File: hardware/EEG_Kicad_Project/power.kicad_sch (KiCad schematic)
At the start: 32 parts, among them U2 TPS60403DBV, U4 TPS73225DBVT, U5 TLV75709PDBV, U6 TPS72325DBVT

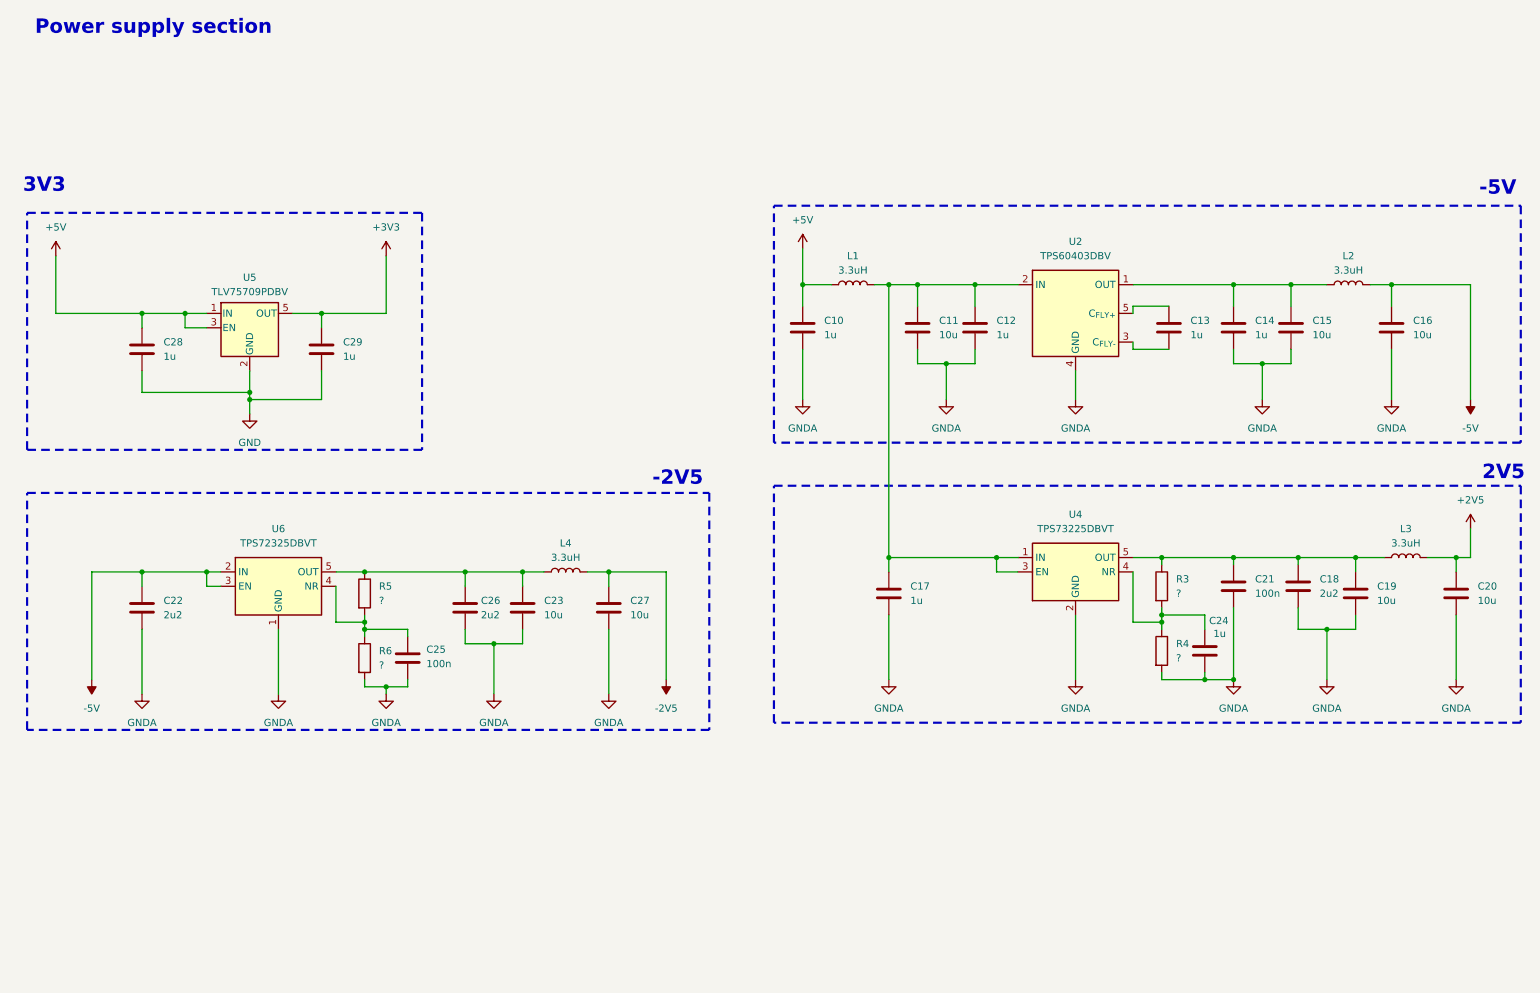
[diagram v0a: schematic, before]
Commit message: Add USB galvanic isolation barrier for patient safety
Adds a USB-C receptacle -> ESD protection -> ADuM3160 isolator ->
isolated TMU3-0511 DC-DC chain, separating the STM32/ADS1299/analog
supply (now fully isolated) from the non-isolated USB-connector side.
Closes the previously-floating USB_OTG_FS_DP/DM pins on the STM32,
adds CC1/CC2 pulldowns and VBUS decoupling on the new receptacle, and
fixes ADuM3160 VBUS2 tie per datasheet. Verified via kicad-happy: no
ERC regressions, isolation barrier confirmed intact (no net bridges
GND_PRI/+5V_PRI with the isolated GNDA/+5V/+3V3 domain).

Co-Authored-By: Claude Sonnet 5 <noreply@anthropic.com>
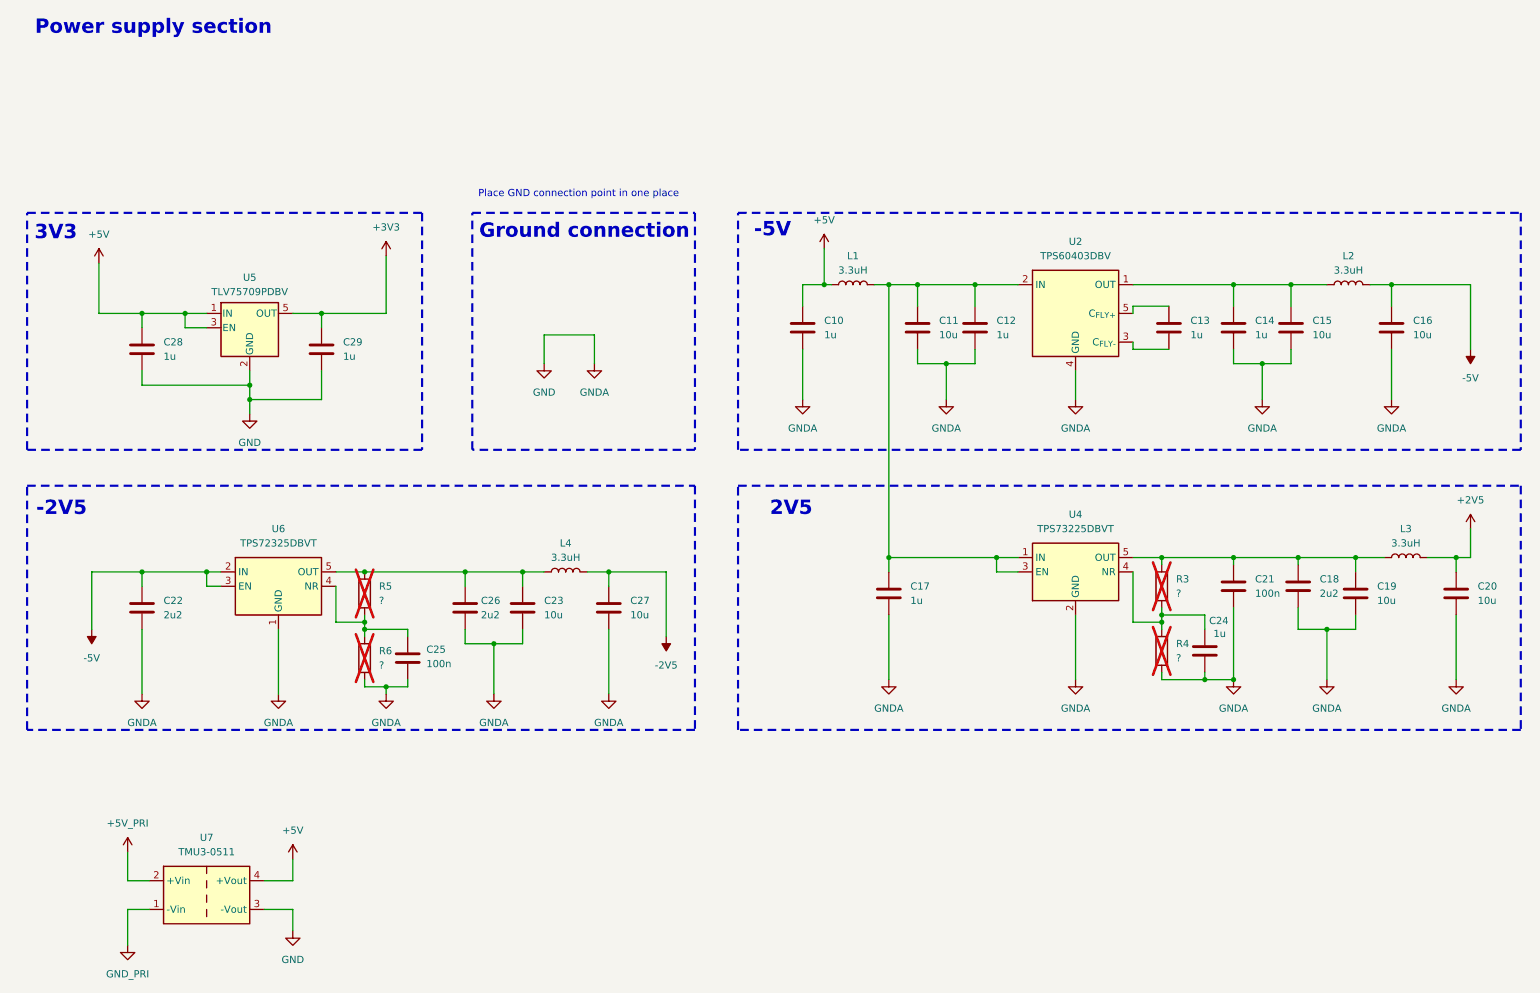
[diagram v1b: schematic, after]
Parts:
- added U7: TMU3-0511, Converter_DCDC:Converter_DCDC_TRACO_TMU3-05xx_12xx_THT, symbol Converter_DCDC:TMU3-0511
- R3, R4, R5, R6: now not fitted; now left out of the parts list
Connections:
- net GNDA is gone; now on net GND: C10.2, C11.2, C12.2, C14.2, C15.2, C16.2, C17.2, C18.2, C19.2, C20.2, C21.2, C22.2, C23.2, C24.2, C25.2, C26.2, C27.2, R4.2, R6.2, U2.4 (GND), U4.2 (GND), U6.1 (GND)
- net +5V: now also U7.4 (+Vout)
- net GND: now also U7.3 (-Vout)
- new net +5V_PRI: U7.2 (+Vin)
- new net GND_PRI: U7.1 (-Vin)
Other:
- note added: "Ground connection"
- note added: "Place GND connection point in one place"
